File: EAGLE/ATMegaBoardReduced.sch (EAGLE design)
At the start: 17 parts, among them IC2 ATMEGA168-20P, IC3 REG1117, X1 49S/18PF

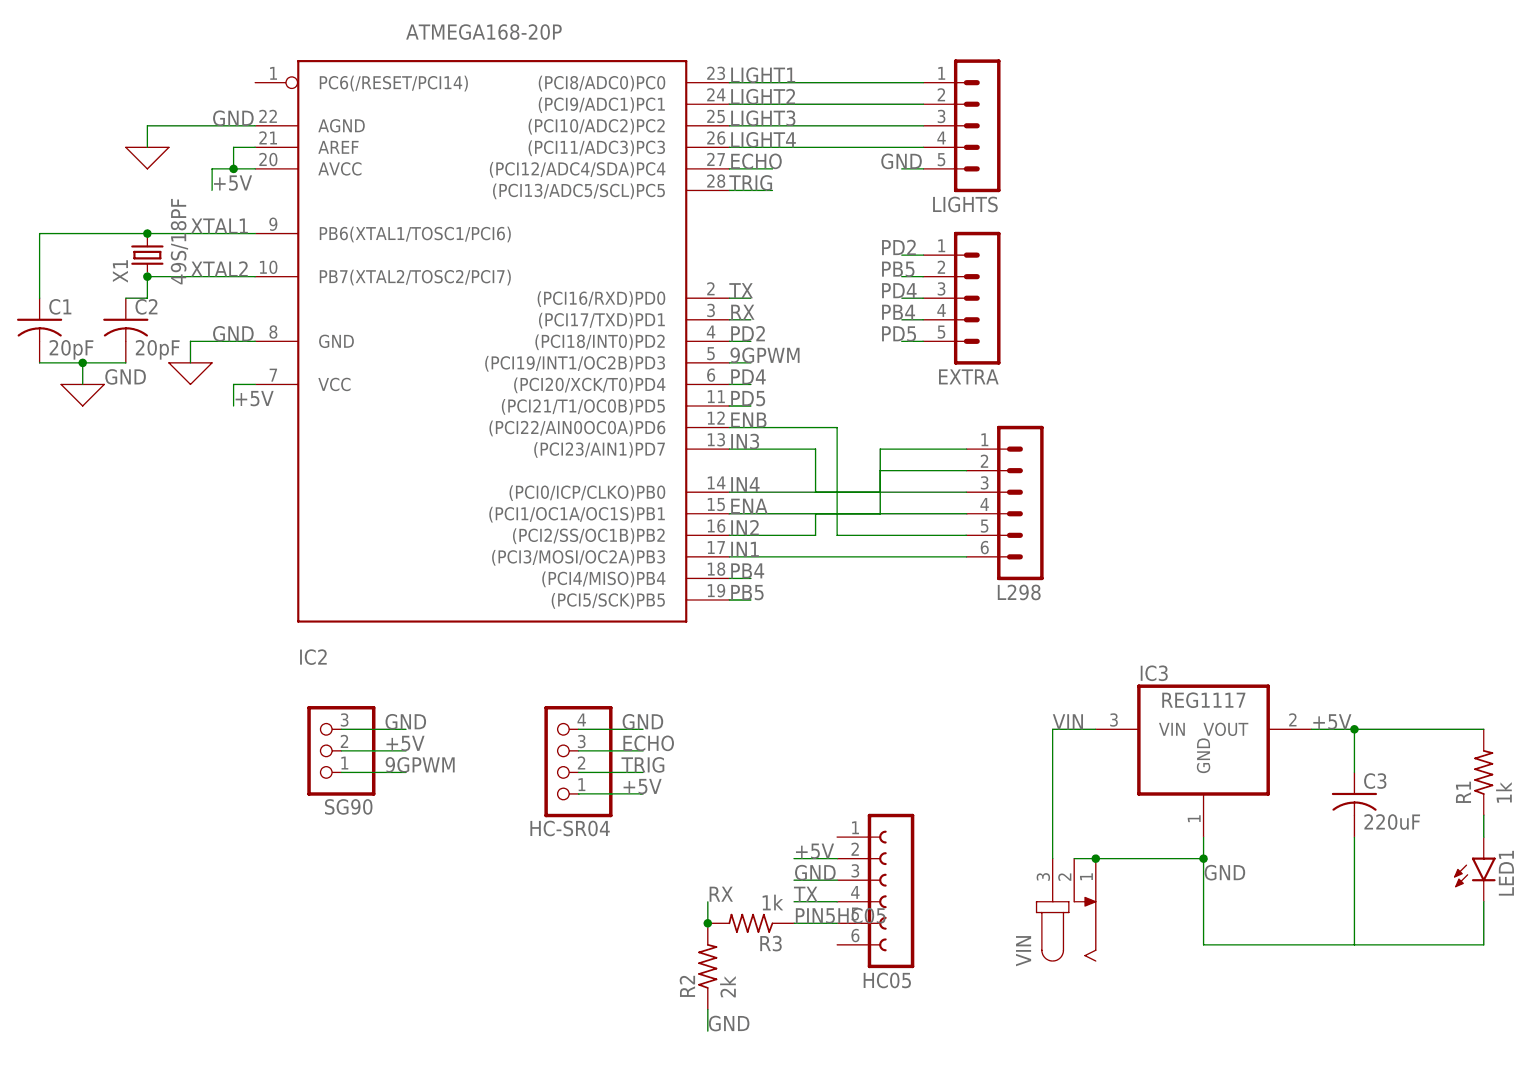
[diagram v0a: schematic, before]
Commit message: set reset pin high added ground pins
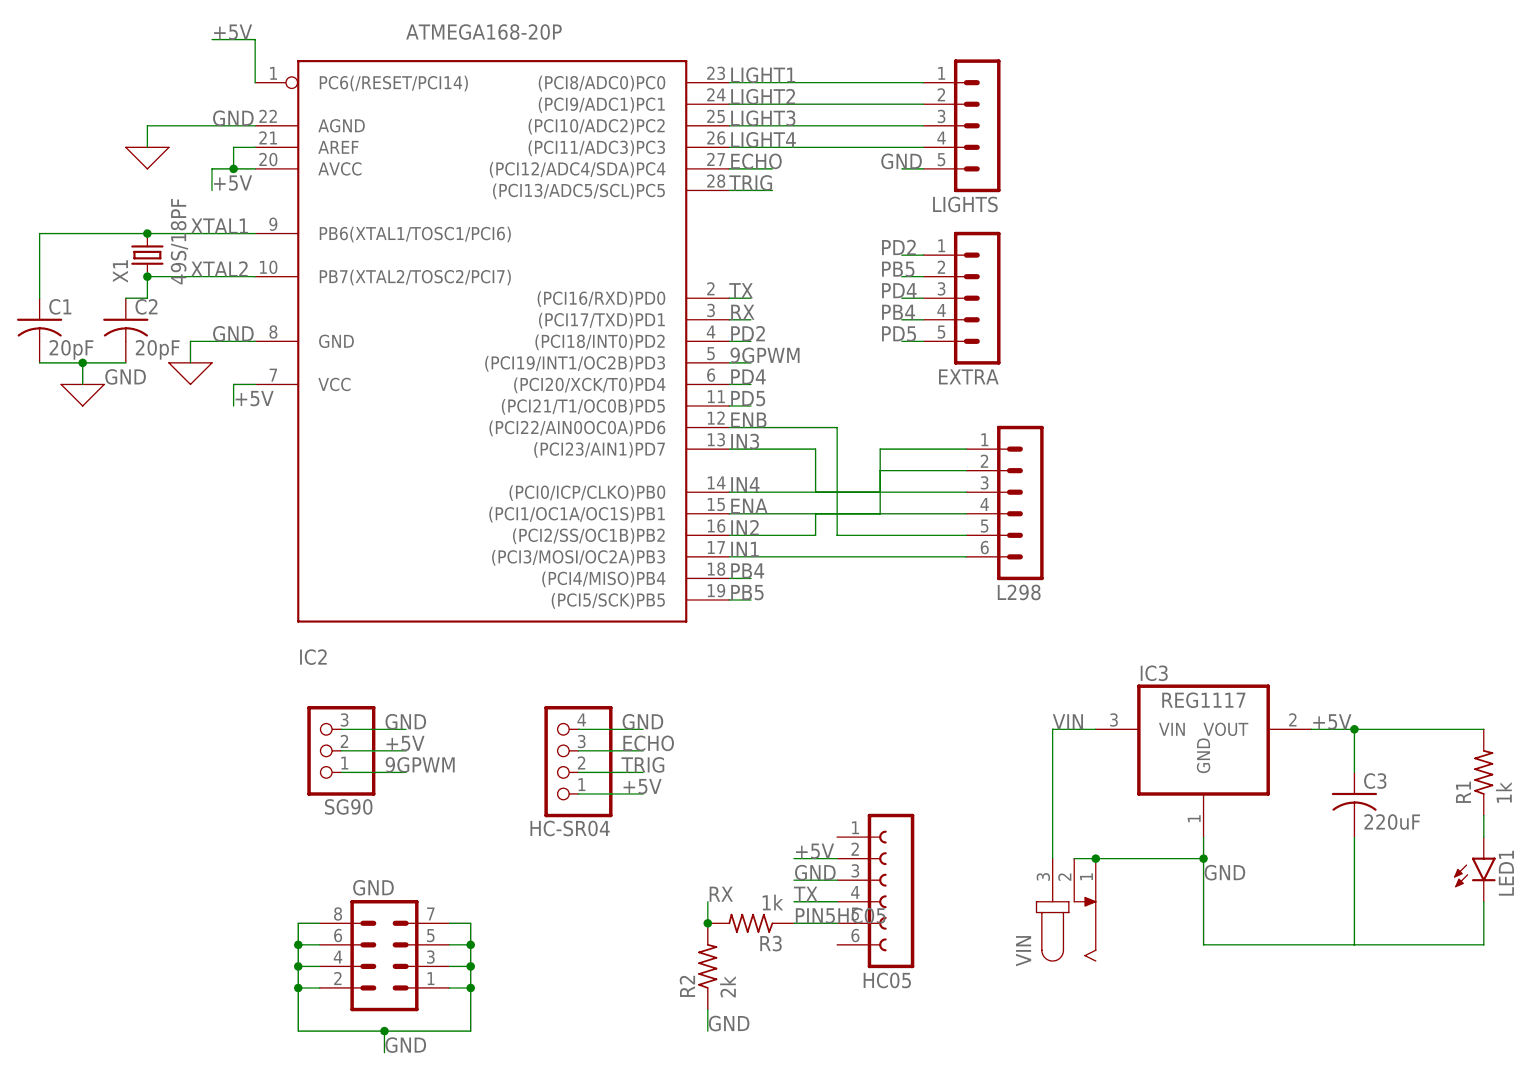
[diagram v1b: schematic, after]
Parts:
- added GND: (no value), con-lstb:MA04-2
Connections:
- net +5V: now also IC2.PC6(/RESET/PCI14)
- net GND: now also GND.1, GND.2, GND.3, GND.4, GND.5, GND.6, GND.7, GND.8
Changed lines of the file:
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@@
 <part name="LIGHTS" library="con-lstb" library_urn="urn:adsk.eagle:library:162" deviceset="MA05-1" device="" package3d_urn="urn:adsk.eagle:package:8332/1"/>
 <part name="EXTRA" library="con-lstb" library_urn="urn:adsk.eagle:library:162" deviceset="MA05-1" device="" package3d_urn="urn:adsk.eagle:package:8332/1"/>
+<part name="GND" library="con-lstb" library_urn="urn:adsk.eagle:library:162" deviceset="MA04-2" device="" package3d_urn="urn:adsk.eagle:package:8368/1"/>
 </parts>
 <sheets>
@@
 <attribute name="NAME" x="120.65" y="44.958" size="1.778" layer="95" rot="R180"/>
 </instance>
+<instance part="GND" gate="G$1" x="48.26" y="-22.86" smashed="yes">
+<attribute name="VALUE" x="44.45" y="-33.02" size="1.778" layer="96"/>
+<attribute name="NAME" x="44.45" y="-17.018" size="1.778" layer="95"/>
+</instance>
 </instances>
 <busses>
@@
 <wire x1="101.6" y1="-12.7" x2="96.52" y2="-12.7" width="0.1524" layer="91"/>
 <label x="96.52" y="-12.7" size="1.778" layer="95"/>
+</segment>
+<segment>
+<pinref part="IC2" gate="G$1" pin="PC6(/RESET/PCI14)"/>
+<wire x1="33.02" y1="78.74" x2="33.02" y2="83.82" width="0.1524" layer="91"/>
+<wire x1="33.02" y1="83.82" x2="27.94" y2="83.82" width="0.1524" layer="91"/>
+<label x="27.94" y="83.82" size="1.778" layer="95"/>
 </segment>
 </net>
@@
 <label x="106.68" y="68.58" size="1.778" layer="95"/>
 </segment>
-</net>
+<segment>
+<wire x1="40.64" y1="-22.86" x2="38.1" y2="-22.86" width="0.1524" layer="91"/>
+<wire x1="38.1" y1="-22.86" x2="38.1" y2="-25.4" width="0.1524" layer="91"/>
+<wire x1="38.1" y1="-25.4" x2="40.64" y2="-25.4" width="0.1524" layer="91"/>
+<wire x1="40.64" y1="-27.94" x2="38.1" y2="-27.94" width="0.1524" layer="91"/>
+<wire x1="38.1" y1="-27.94" x2="38.1" y2="-25.4" width="0.1524" layer="91"/>
+<junction x="38.1" y="-25.4"/>
+<wire x1="38.1" y1="-27.94" x2="38.1" y2="-33.02" width="0.1524" layer="91"/>
+<junction x="38.1" y="-27.94"/>
+<wire x1="55.88" y1="-22.86" x2="58.42" y2="-22.86" width="0.1524" layer="91"/>
+<wire x1="58.42" y1="-22.86" x2="58.42" y2="-25.4" width="0.1524" layer="91"/>
+<wire x1="58.42" y1="-25.4" x2="55.88" y2="-25.4" width="0.1524" layer="91"/>
+<wire x1="55.88" y1="-27.94" x2="58.42" y2="-27.94" width="0.1524" layer="91"/>
+<wire x1="58.42" y1="-27.94" x2="58.42" y2="-25.4" width="0.1524" layer="91"/>
+<junction x="58.42" y="-25.4"/>
+<wire x1="38.1" y1="-33.02" x2="48.26" y2="-33.02" width="0.1524" layer="91"/>
+<wire x1="48.26" y1="-33.02" x2="58.42" y2="-33.02" width="0.1524" layer="91"/>
+<wire x1="58.42" y1="-33.02" x2="58.42" y2="-27.94" width="0.1524" layer="91"/>
+<junction x="58.42" y="-27.94"/>
+<wire x1="48.26" y1="-33.02" x2="48.26" y2="-35.56" width="0.1524" layer="91"/>
+<junction x="48.26" y="-33.02"/>
+<label x="48.26" y="-35.56" size="1.778" layer="95"/>
+<pinref part="GND" gate="G$1" pin="1"/>
+<pinref part="GND" gate="G$1" pin="3"/>
+<pinref part="GND" gate="G$1" pin="5"/>
+<pinref part="GND" gate="G$1" pin="2"/>
+<pinref part="GND" gate="G$1" pin="4"/>
+<pinref part="GND" gate="G$1" pin="6"/>
+<wire x1="38.1" y1="-22.86" x2="38.1" y2="-20.32" width="0.1524" layer="91"/>
+<junction x="38.1" y="-22.86"/>
+<pinref part="GND" gate="G$1" pin="8"/>
+<wire x1="38.1" y1="-20.32" x2="40.64" y2="-20.32" width="0.1524" layer="91"/>
+<wire x1="58.42" y1="-22.86" x2="58.42" y2="-20.32" width="0.1524" layer="91"/>
+<junction x="58.42" y="-22.86"/>
+<pinref part="GND" gate="G$1" pin="7"/>
+<wire x1="58.42" y1="-20.32" x2="55.88" y2="-20.32" width="0.1524" layer="91"/>
+</segment>
+</net>
